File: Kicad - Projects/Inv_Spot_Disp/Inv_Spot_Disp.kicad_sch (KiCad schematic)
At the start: 41 parts, among them J1 PWM_Out, J2 Power_Supply, J3 Current_Sense, J4 Prog, J6 Rail_Sense, SW1 1, SW2 2, SW3 3, SW4 4, SW5 SW_Push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

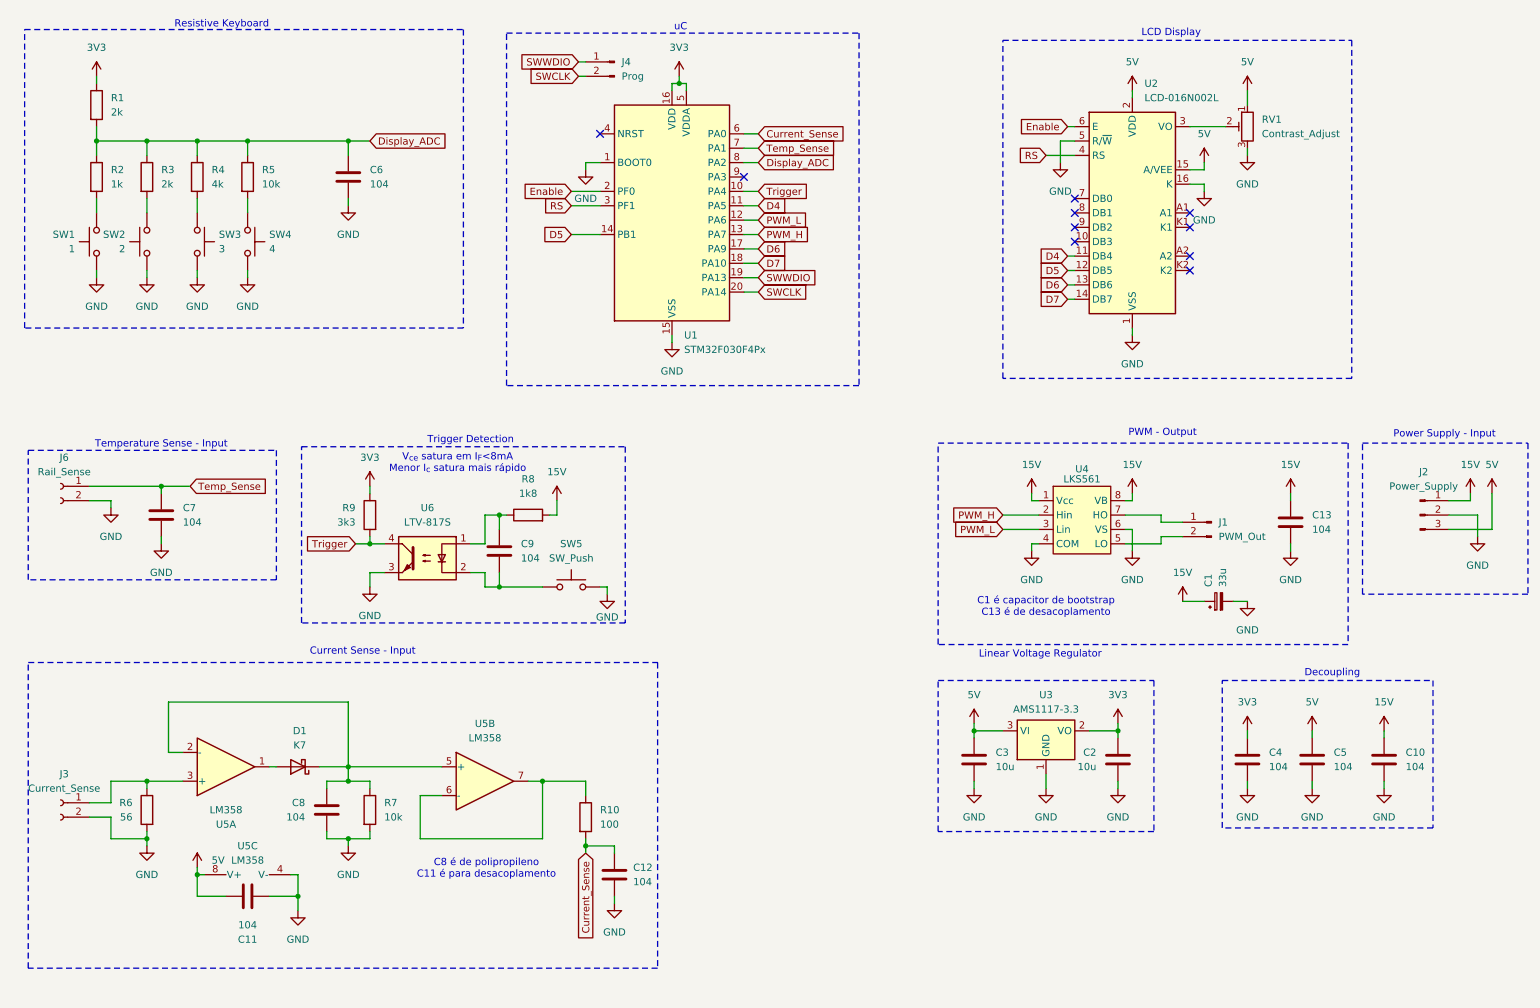
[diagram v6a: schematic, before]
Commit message: Primeiro Layout - Display
Feito o layout preliminar da placa de display, conferir com o Anderson

Corrigido problema com o layout do transformador (erro no símbolo utilizado levou a inversão dos IGBTs superiores)
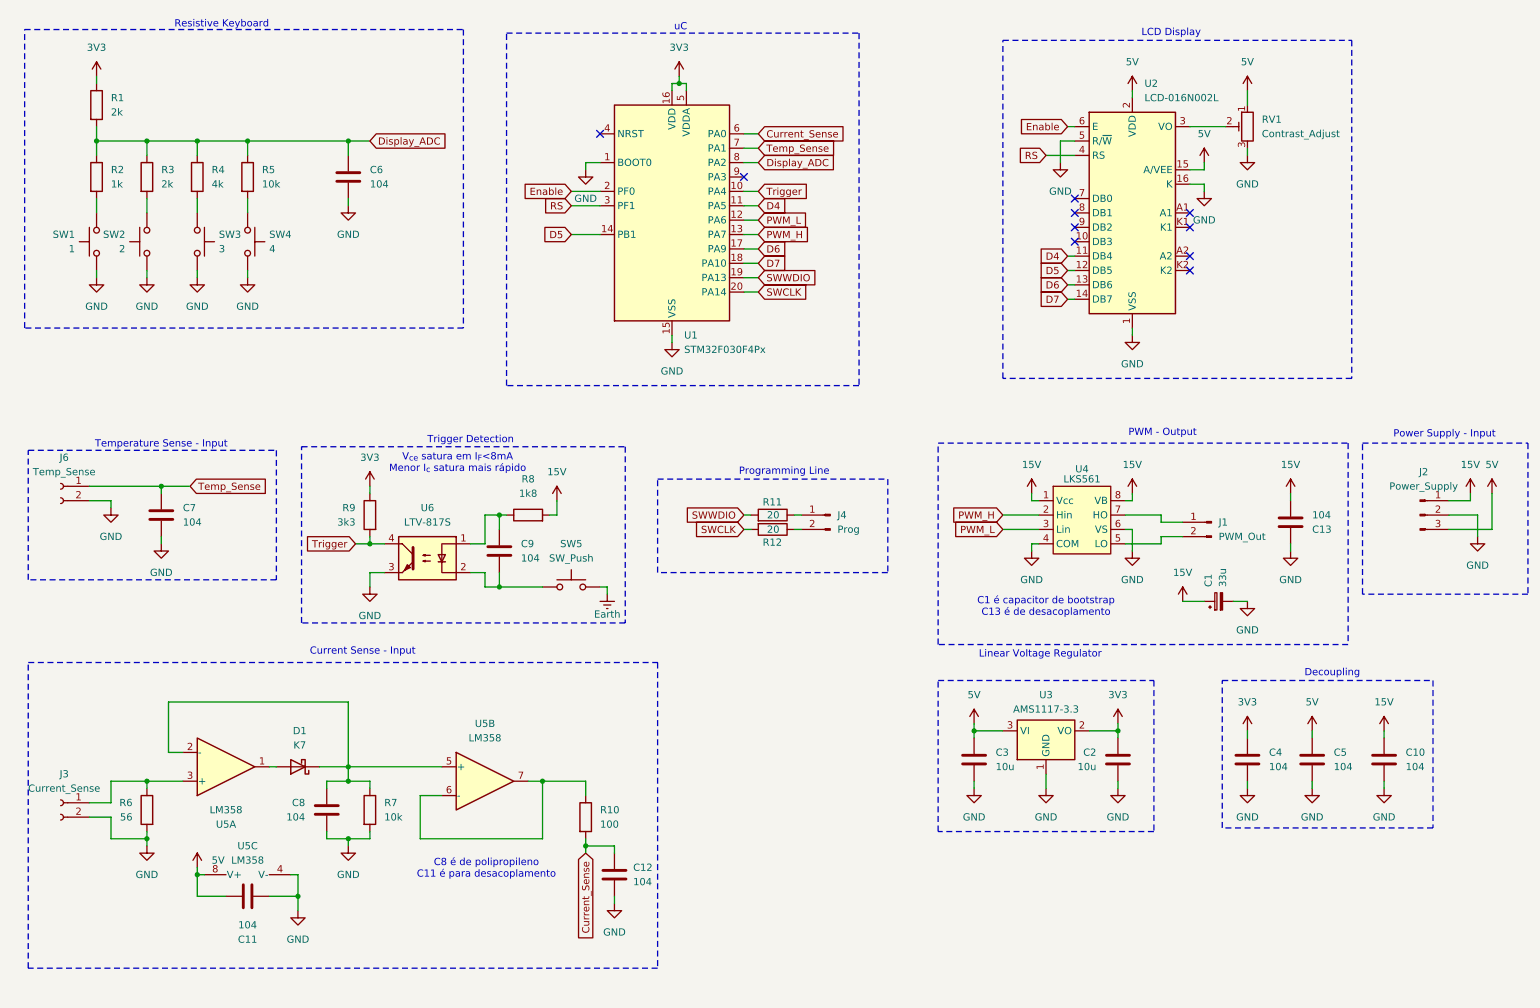
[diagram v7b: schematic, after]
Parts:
- added R11, R12: 20, Resistor_SMD:R_1206_3216Metric_Pad1.30x1.75mm_HandSolder, symbol Device:R
- C2, C3: footprint (none) -> Capacitor_THT:C_Radial_D10.0mm_H12.5mm_P5.00mm
- J6: value Rail_Sense -> Temp_Sense
- U5: footprint (none) -> Package_SO:SOIC-8_3.9x4.9mm_P1.27mm
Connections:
- net 15V: now also C13.2; no longer C13.1
- net GND: now also C13.1; no longer C13.2, SW5.2
- net SWCLK: now also R12.2; no longer J4.2 (Pin_2)
- net SWWDIO: now also R11.2; no longer J4.1 (Pin_1)
- new net: J4.1 (Pin_1), R11.1
- new net: J4.2 (Pin_2), R12.1
- new net Earth: SW5.2
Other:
- note added: "Programming Line"
- moved on the sheet: J4

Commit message: Ajustes Gerais
Ajustes Gerais
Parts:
- removed J4: Prog, Connector_PinHeader_2.00mm:PinHeader_1x02_P2.00mm_Vertical, symbol Connector:Conn_01x02_Pin
- added J4: Prog, Connector_PinHeader_2.00mm:PinHeader_1x04_P2.00mm_Vertical, symbol Connector:Conn_01x04_Pin
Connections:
- net 3V3: now also J4.1 (Pin_1)
- net GND: now also J4.4 (Pin_4)
- net at R11.1: now also J4.2 (Pin_2)
- net at R12.1: now also J4.3 (Pin_3)
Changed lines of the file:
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@@
 	)
 	(rectangle
-		(start 128.27 99.06)
-		(end 168.91 115.57)
+		(start 128.27 92.71)
+		(end 168.91 118.11)
 		(stroke
 			(width 0)
@@
 	(text "Programming Line"
 		(exclude_from_sim no)
-		(at 150.622 97.79 0)
+		(at 148.336 91.186 0)
 		(effects
 			(font
@@
 	(wire
 		(pts
+			(xy 153.67 102.87) (xy 152.4 102.87)
+		)
+		(stroke
+			(width 0)
+			(type default)
+		)
+	)
+	(wire
+		(pts
 			(xy 73.66 39.37) (xy 73.66 41.91)
 		)
@@
 	(wire
 		(pts
+			(xy 152.4 102.87) (xy 152.4 101.6)
+		)
+		(stroke
+			(width 0)
+			(type default)
+		)
+	)
+	(wire
+		(pts
 			(xy 146.05 66.04) (xy 143.51 66.04)
 		)
@@
 	(wire
 		(pts
+			(xy 153.67 110.49) (xy 152.4 110.49)
+		)
+		(stroke
+			(width 0)
+			(type default)
+		)
+	)
+	(wire
+		(pts
 			(xy 64.77 168.91) (xy 64.77 172.72)
 		)
@@
 	(wire
 		(pts
+			(xy 152.4 110.49) (xy 152.4 111.76)
+		)
+		(stroke
+			(width 0)
+			(type default)
+		)
+	)
+	(wire
+		(pts
 			(xy 273.05 105.41) (xy 273.05 109.22)
 		)
@@
 	)
 	(symbol
-		(lib_id "Connector:Conn_01x02_Pin")
-		(at 158.75 105.41 0)
-		(mirror y)
-		(unit 1)
-		(body_style 1)
-		(exclude_from_sim no)
-		(in_bom yes)
-		(on_board yes)
-		(in_pos_files yes)
-		(dnp no)
-		(fields_autoplaced yes)
-		(property "Reference" "J4"
-			(at 160.02 105.4099 0)
-			(show_name no)
-			(do_not_autoplace no)
-			(effects
-				(font
-					(size 1.27 1.27)
-				)
-				(justify right)
-			)
-		)
-		(property "Value" "Prog"
-			(at 160.02 107.9499 0)
-			(show_name no)
-			(do_not_autoplace no)
-			(effects
-				(font
-					(size 1.27 1.27)
-				)
-				(justify right)
-			)
-		)
-		(property "Footprint" "Connector_PinHeader_2.00mm:PinHeader_1x02_P2.00mm_Vertical"
-			(at 158.75 105.41 0)
-			(hide yes)
-			(show_name no)
-			(do_not_autoplace no)
-			(effects
-				(font
-					(size 1.27 1.27)
-				)
-			)
-		)
-		(property "Datasheet" ""
-			(at 158.75 105.41 0)
-			(hide yes)
-			(show_name no)
-			(do_not_autoplace no)
-			(effects
-				(font
-					(size 1.27 1.27)
-				)
-			)
-		)
-		(property "Description" "Generic connector, single row, 01x02, script generated"
-			(at 158.75 105.41 0)
-			(hide yes)
-			(show_name no)
-			(do_not_autoplace no)
-			(effects
-				(font
-					(size 1.27 1.27)
-				)
-			)
-		)
-		(pin "1"
-		)
-		(pin "2"
-		)
-		(instances
-			(project "Inv_Spot_Disp"
-				(path "/016976b8-e488-405d-b5a2-1b3e7431e7ce"
-					(reference "J4")
-					(unit 1)
-				)
-			)
-		)
-	)
-	(symbol
 		(lib_id "power:VCC")
 		(at 232.41 30.48 0)
@@
 	)
 	(symbol
+		(lib_id "power:VCC")
+		(at 152.4 101.6 0)
+		(unit 1)
+		(body_style 1)
+		(exclude_from_sim no)
+		(in_bom yes)
+		(on_board yes)
+		(in_pos_files yes)
+		(dnp no)
+		(fields_autoplaced yes)
+		(property "Reference" "#PWR023"
+			(at 152.4 105.41 0)
+			(hide yes)
+			(show_name no)
+			(do_not_autoplace no)
+			(effects
+				(font
+					(size 1.27 1.27)
+				)
+			)
+		)
+		(property "Value" "3V3"
+			(at 152.4 96.52 0)
+			(show_name no)
+			(do_not_autoplace no)
+			(effects
+				(font
+					(size 1.27 1.27)
+				)
+			)
+		)
+		(property "Footprint" ""
+			(at 152.4 101.6 0)
+			(hide yes)
+			(show_name no)
+			(do_not_autoplace no)
+			(effects
+				(font
+					(size 1.27 1.27)
+				)
+			)
+		)
+		(property "Datasheet" ""
+			(at 152.4 101.6 0)
+			(hide yes)
+			(show_name no)
+			(do_not_autoplace no)
+			(effects
+				(font
+					(size 1.27 1.27)
+				)
+			)
+		)
+		(property "Description" "Power symbol creates a global label with name \"VCC\""
+			(at 152.4 101.6 0)
+			(hide yes)
+			(show_name no)
+			(do_not_autoplace no)
+			(effects
+				(font
+					(size 1.27 1.27)
+				)
+			)
+		)
+		(pin "1"
+		)
+		(instances
+			(project "Inv_Spot_Disp"
+				(path "/016976b8-e488-405d-b5a2-1b3e7431e7ce"
+					(reference "#PWR023")
+					(unit 1)
+				)
+			)
+		)
+	)
+	(symbol
 		(lib_id "power:GND")
 		(at 29.21 63.5 0)
@@
 	)
 	(symbol
+		(lib_id "power:GND")
+		(at 152.4 111.76 0)
+		(unit 1)
+		(body_style 1)
+		(exclude_from_sim no)
+		(in_bom yes)
+		(on_board yes)
+		(in_pos_files yes)
+		(dnp no)
+		(fields_autoplaced yes)
+		(property "Reference" "#PWR022"
+			(at 152.4 118.11 0)
+			(hide yes)
+			(show_name no)
+			(do_not_autoplace no)
+			(effects
+				(font
+					(size 1.27 1.27)
+				)
+			)
+		)
+		(property "Value" "GND"
+			(at 152.4 116.84 0)
+			(show_name no)
+			(do_not_autoplace no)
+			(effects
+				(font
+					(size 1.27 1.27)
+				)
+			)
+		)
+		(property "Footprint" ""
+			(at 152.4 111.76 0)
+			(hide yes)
+			(show_name no)
+			(do_not_autoplace no)
+			(effects
+				(font
+					(size 1.27 1.27)
+				)
+			)
+		)
+		(property "Datasheet" ""
+			(at 152.4 111.76 0)
+			(hide yes)
+			(show_name no)
+			(do_not_autoplace no)
+			(effects
+				(font
+					(size 1.27 1.27)
+				)
+			)
+		)
+		(property "Description" "Power symbol creates a global label with name \"GND\" , ground"
+			(at 152.4 111.76 0)
+			(hide yes)
+			(show_name no)
+			(do_not_autoplace no)
+			(effects
+				(font
+					(size 1.27 1.27)
+				)
+			)
+		)
+		(pin "1"
+		)
+		(instances
+			(project "Inv_Spot_Disp"
+				(path "/016976b8-e488-405d-b5a2-1b3e7431e7ce"
+					(reference "#PWR022")
+					(unit 1)
+				)
+			)
+		)
+	)
+	(symbol
 		(lib_id "Device:C")
 		(at 120.65 168.91 0)
@@
 					(unit 1)
 				)
+			)
+		)
+	)
+	(symbol
+		(lib_id "Connector:Conn_01x04_Pin")
+		(at 158.75 105.41 0)
+		(mirror y)
+		(unit 1)
+		(body_style 1)
+		(exclude_from_sim no)
+		(in_bom yes)
+		(on_board yes)
+		(in_pos_files yes)
+		(dnp no)
+		(fields_autoplaced yes)
+		(property "Reference" "J4"
+			(at 160.02 105.4099 0)
+			(show_name no)
+			(do_not_autoplace no)
+			(effects
+				(font
+					(size 1.27 1.27)
+				)
+				(justify right)
+			)
+		)
+		(property "Value" "Prog"
+			(at 160.02 107.9499 0)
+			(show_name no)
+			(do_not_autoplace no)
+			(effects
+				(font
+					(size 1.27 1.27)
+				)
+				(justify right)
+			)
+		)
+		(property "Footprint" "Connector_PinHeader_2.00mm:PinHeader_1x04_P2.00mm_Vertical"
+			(at 158.75 105.41 0)
+			(hide yes)
+			(show_name no)
+			(do_not_autoplace no)
+			(effects
+				(font
+					(size 1.27 1.27)
+				)
+			)
+		)
+		(property "Datasheet" ""
+			(at 158.75 105.41 0)
+			(hide yes)
+			(show_name no)
+			(do_not_autoplace no)
+			(effects
+				(font
+					(size 1.27 1.27)
+				)
+			)
+		)
+		(property "Description" "Generic connector, single row, 01x04, script generated"
+			(at 158.75 105.41 0)
+			(hide yes)
+			(show_name no)
+			(do_not_autoplace no)
+			(effects
+				(font
+					(size 1.27 1.27)
+				)
+			)
+		)
+		(pin "1"
+		)
+		(pin "4"
+		)
+		(pin "2"
+		)
+		(pin "3"
+		)
+		(instances
+			(project "Inv_Spot_Disp"
+				(path "/016976b8-e488-405d-b5a2-1b3e7431e7ce"
+					(reference "J4")
+					(unit 1)
+				)
